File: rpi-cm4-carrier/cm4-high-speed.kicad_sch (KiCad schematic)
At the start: 5 parts, among them J4 USB_OTG, U6 D3V3F4U10LP-7

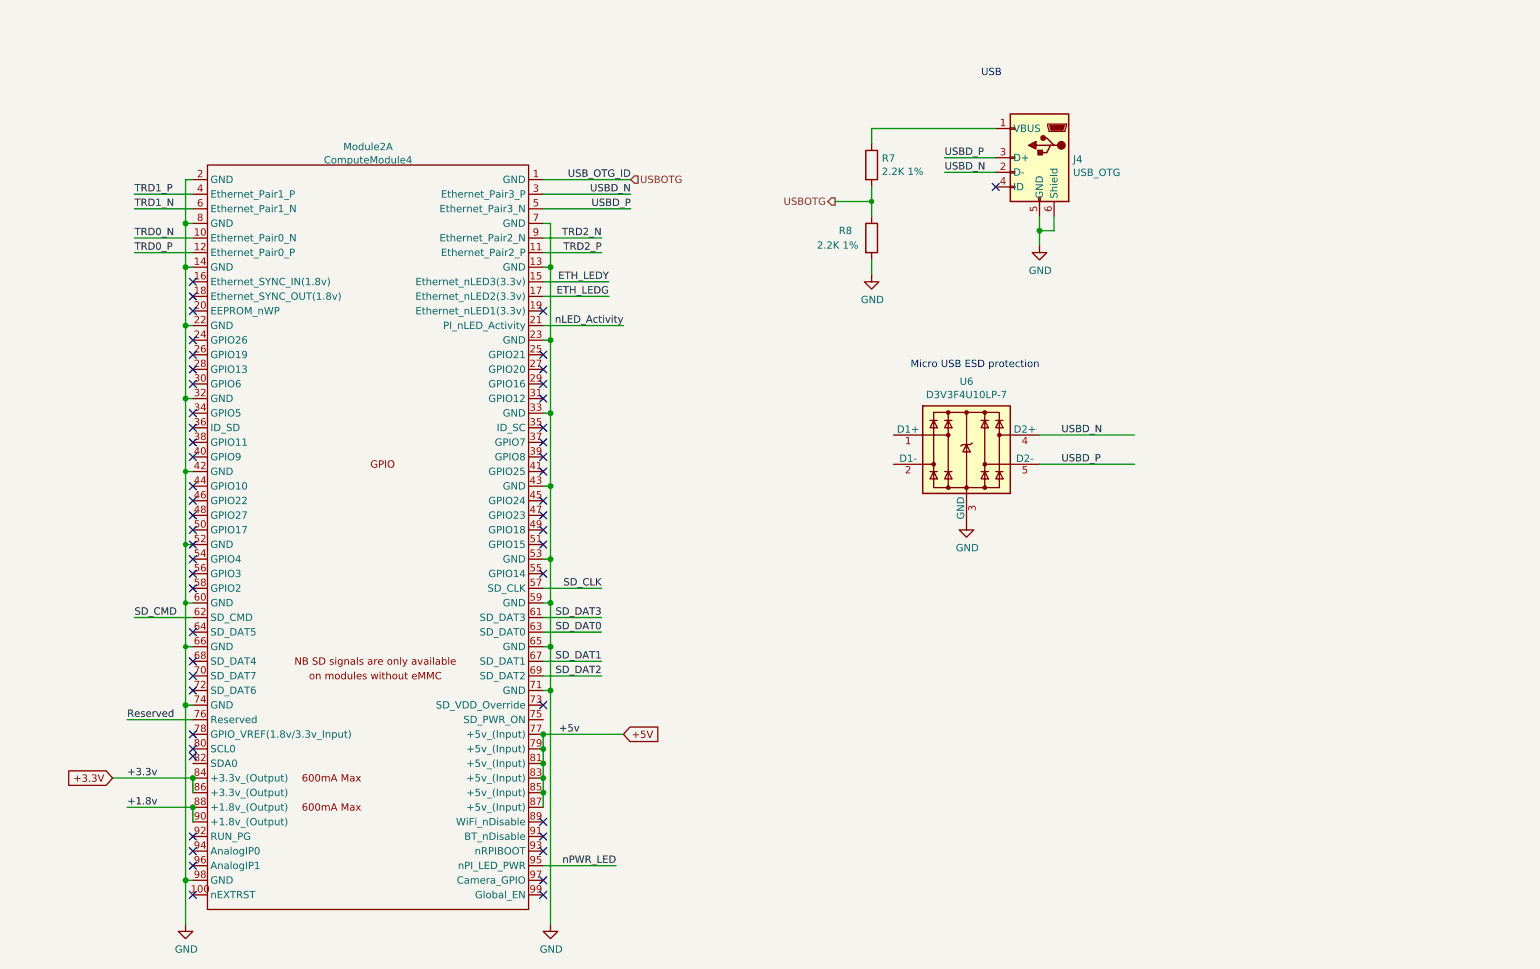
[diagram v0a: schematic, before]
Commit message: Wired Ethernet data
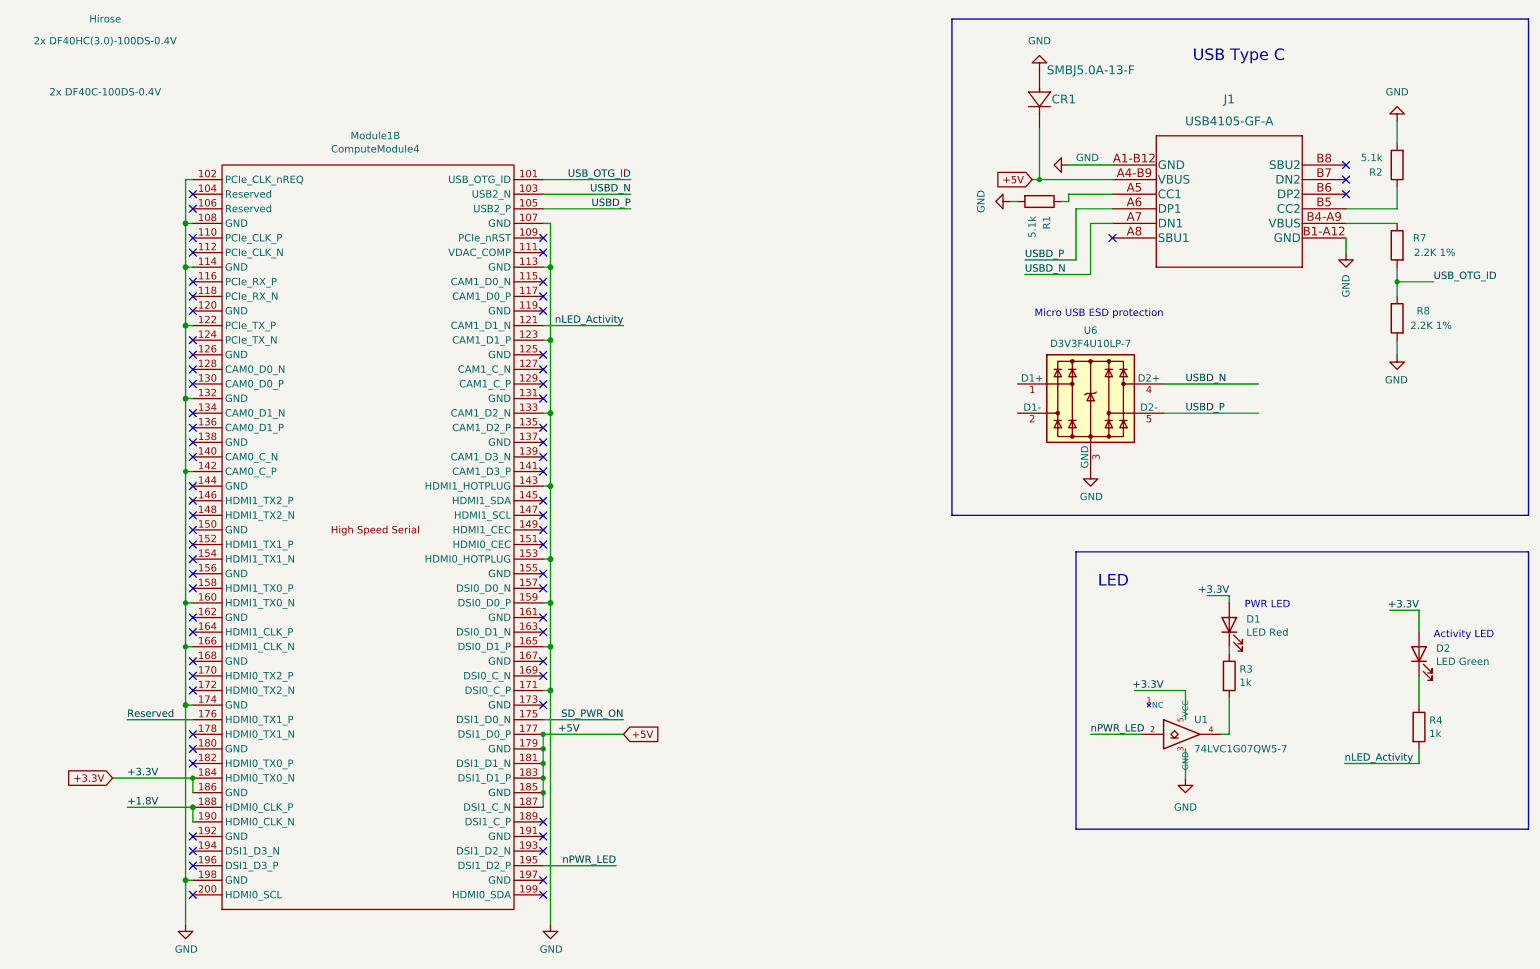
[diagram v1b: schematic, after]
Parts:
- removed J4: USB_OTG, CM4IO:USB_Micro-B_EDAC_UCON00686, symbol Connector:USB_OTG
- added CR1: SMBJ5.0A-13-F, Diode_SMD:D_SMB, symbol SMBJ5.0A-13-F:SMBJ5.0A-13-F
- added D1: LED Red, LED_SMD:LED_0603_1608Metric, symbol Device:LED
- added D2: LED Green, LED_SMD:LED_0603_1608Metric, symbol Device:LED
- added J1: USB4105-GF-A, USB4105-GF-A:USB4105-GF-A, symbol USB4105-GF-A:USB4105-GF-A
- added R1, R2: 5.1k, Resistor_SMD:R_0201_0603Metric_Pad0.64x0.40mm_HandSolder, symbol Device:R
- added R3, R4: 1k, Resistor_SMD:R_0402_1005Metric, symbol Device:R
- added U1: 74LVC1G07QW5-7, Package_TO_SOT_SMD:SOT-353_SC-70-5, symbol CM4IO:74LVC1G07_copy
- Module1: renamed from Module2; Digi-Key_PN (none) -> 2x H11615CT-ND; Digi-Key_PN (Alt) (none) -> 2x H124602CT-ND; MPN (none) -> 2x DF40C-100DS-0.4V; MPN (Alt) (none) -> 2x DF40HC(3.0)-100DS-0.4V; Manufacturer (none) -> Hirose
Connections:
- net +3.3V: now also Module1.184 (HDMI0_TX0_N), Module1.186 (GND), D1.2 (A), D2.2 (A), U1.5 (VCC); no longer Module1.84 (+3.3v_(Output)), Module1.86 (+3.3v_(Output))
- net +5V: now also Module1.177 (DSI1_D0_P), Module1.179 (GND), Module1.181 (DSI1_D1_N), Module1.183 (DSI1_D1_P), Module1.185 (GND), Module1.187 (DSI1_C_N), CR1.1, J1.A4-B9 (VBUS); no longer Module1.77 (+5v_(Input)), Module1.79 (+5v_(Input)), Module1.81 (+5v_(Input)), Module1.83 (+5v_(Input)), Module1.85 (+5v_(Input)), Module1.87 (+5v_(Input))
- net GND: now also Module1.102 (PCIe_CLK_nREQ), Module1.107 (GND), Module1.108 (GND), Module1.113 (GND), Module1.114 (GND), Module1.122 (PCIe_TX_P), Module1.123 (CAM1_D1_P), Module1.132 (GND), Module1.133 (CAM1_D2_N), Module1.142 (CAM0_C_P), Module1.143 (HDMI1_HOTPLUG), Module1.153 (HDMI0_HOTPLUG), Module1.159 (DSI0_D0_P), Module1.160 (HDMI1_TX0_N), Module1.165 (DSI0_D1_P), Module1.166 (HDMI1_CLK_N), Module1.171 (DSI0_C_P), Module1.174 (GND), Module1.198 (GND), CR1.2, J1.A1-B12 (GND), J1.B1-A12 (GND), R1.2, R2.2, U1.3 (GND); no longer Module1.13 (GND), Module1.14 (GND), Module1.2 (GND), Module1.22 (GND), Module1.23 (GND), Module1.32 (GND), Module1.33 (GND), Module1.42 (GND), Module1.43 (GND), Module1.52 (GND), Module1.53 (GND), Module1.59 (GND), Module1.60 (GND), Module1.65 (GND), Module1.66 (GND), Module1.7 (GND), Module1.71 (GND), Module1.74 (GND), Module1.8 (GND), Module1.98 (GND)
- net Reserved: now also Module1.176 (HDMI0_TX1_P); no longer Module1.76 (Reserved)
- net USBD_N: now also Module1.103 (USB2_N), J1.A7 (DN1); no longer Module1.3 (Ethernet_Pair3_P)
- net USBD_P: now also Module1.105 (USB2_P), J1.A6 (DP1); no longer Module1.5 (Ethernet_Pair3_N)
- net nLED_Activity: now also Module1.121 (CAM1_D1_N), R4.2; no longer Module1.21 (PI_nLED_Activity)
- net nPWR_LED: now also Module1.195 (DSI1_D2_P), U1.2; no longer Module1.95 (nPI_LED_PWR)
- net at R7.1: now also J1.B4-A9 (VBUS)
- removed net +1.8v: Module1.88 (+1.8v_(Output)), Module1.90 (+1.8v_(Output))
- removed net ETH_LEDG: Module1.17 (Ethernet_nLED2(3.3v))
- removed net ETH_LEDY: Module1.15 (Ethernet_nLED3(3.3v))
- removed net SD_CLK: Module1.57 (SD_CLK)
- removed net SD_CMD: Module1.62 (SD_CMD)
- removed net SD_DAT0: Module1.63 (SD_DAT0)
- removed net SD_DAT1: Module1.67 (SD_DAT1)
- removed net SD_DAT2: Module1.69 (SD_DAT2)
- removed net SD_DAT3: Module1.61 (SD_DAT3)
- removed net TRD0_N: Module1.10 (Ethernet_Pair0_N)
- removed net TRD0_P: Module1.12 (Ethernet_Pair0_P)
- removed net TRD1_N: Module1.6 (Ethernet_Pair1_N)
- removed net TRD1_P: Module1.4 (Ethernet_Pair1_P)
- removed net TRD2_N: Module1.9 (Ethernet_Pair2_N)
- removed net TRD2_P: Module1.11 (Ethernet_Pair2_P)
- net USBOTG renamed USB_OTG_ID
- net USB_OTG_ID: now also Module1.101 (USB_OTG_ID); no longer Module1.1 (GND)
- new net: J1.A5 (CC1), R1.1
- new net: J1.B5 (CC2), R2.1
- new net: D2.1 (K), R4.1
- new net: D1.1 (K), R3.1
- new net: R3.2, U1.4
- new net +1.8V: Module1.188 (HDMI0_CLK_P), Module1.190 (HDMI0_CLK_N)
- new net SD_PWR_ON: Module1.175 (DSI1_D0_N)
- no-connect marks 51 -> 68
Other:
- note added: "Activity LED"
- note added: "LED"
- note added: "PWR LED"
- note added: "USB Type C"
- note removed: "USB"
- moved on the sheet: U6
